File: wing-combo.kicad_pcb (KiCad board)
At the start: 2 copper layers, 93 x 91.3 mm, 118 parts, among them J1 Conn_01x03_Male, J10 Screw_Terminal_01x02, J11 Screw_Terminal_01x02, J12 Screw_Terminal_01x02, J13 USB_A, J14 Screw_Terminal_01x02, J15 Conn_02x16_Row_Letter_Last, J16 Conn_02x12_Row_Letter_Last, J5 Screw_Terminal_01x02, J6 Screw_Terminal_01x02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

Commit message: change URL on board to makehaven.org/toolauth, to match with Project name on GitHub
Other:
- board text added: "makehaven.org/toolauth"
- board text removed: "makehaven.org/openshop"
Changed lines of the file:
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@@
 		)
 	)
-	(gr_text "makehaven.org/openshop"
-		(at 68.435 53.46 90)
+	(gr_text "makehaven.org/toolauth"
+		(at 68.435 53.579828 90)
 		(layer "B.SilkS")
 		(effects

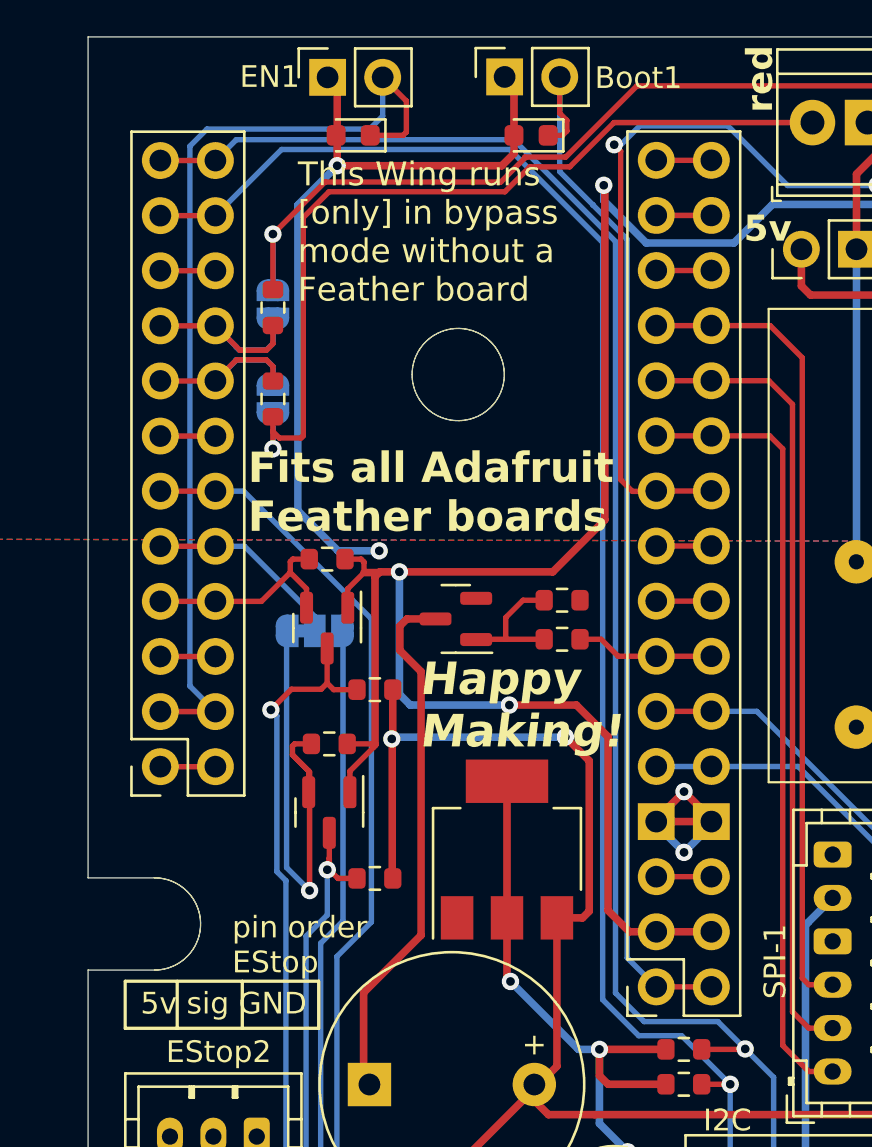
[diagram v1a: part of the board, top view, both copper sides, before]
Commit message: unpopulate headers that are not needed
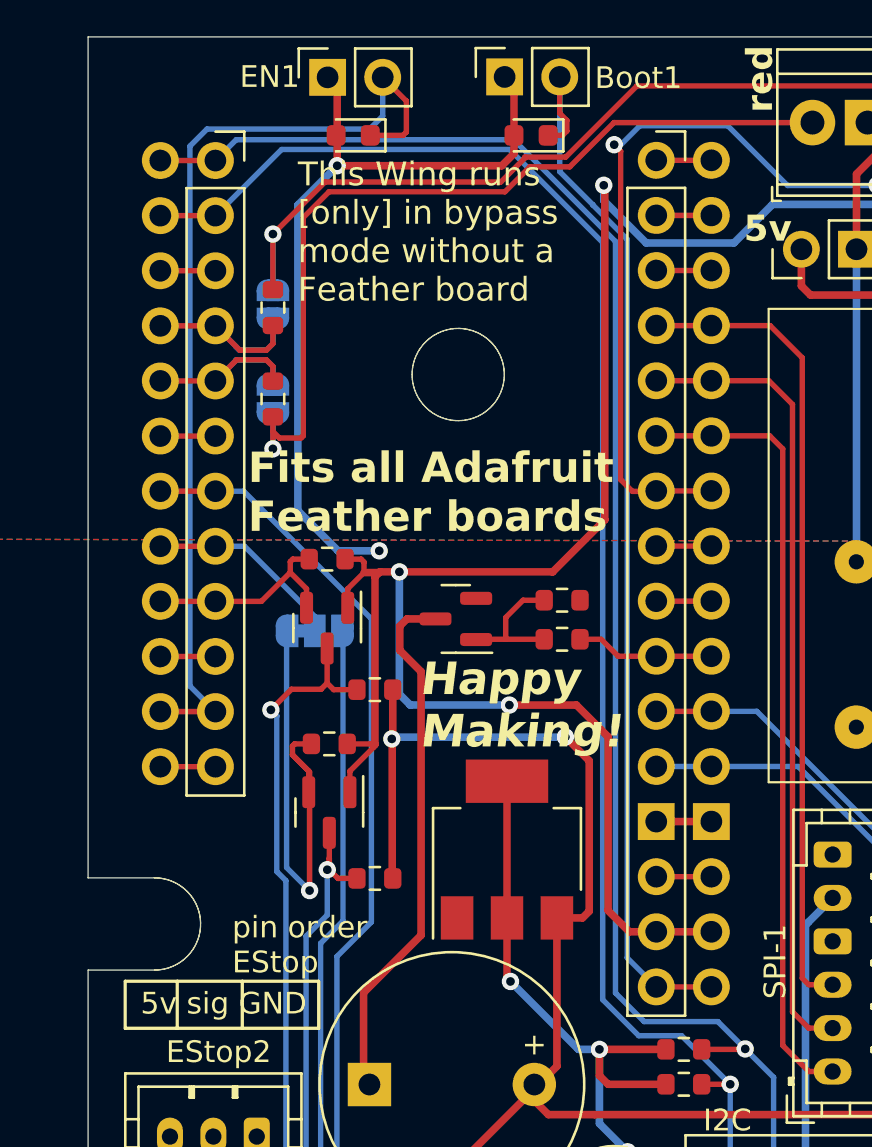
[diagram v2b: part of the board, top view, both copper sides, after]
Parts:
- added J3: Conn_01x12, Connector_PinSocket_2.54mm:PinSocket_1x12_P2.54mm_Vertical, F.Cu at (42.8, 28.6)
- added J4: Conn_01x12, Connector_PinSocket_2.54mm:PinSocket_1x12_P2.54mm_Vertical, F.Cu at (40.2, 28.6)
- IN-1: value 3.5mm -> H/L1
- IN-2: value 3.5mm -> N/L2
- IN-3: value 3.5mm -> VOLTS
- J15: value Conn_02x16_Row_Letter_Last -> Conn_01x16; footprint Connector_PinSocket_2.54mm:PinSocket_2x16_P2.54mm_Vertical -> Connector_PinSocket_2.54mm:PinSocket_1x16_P2.54mm_Vertical
- J16: value Conn_02x12_Row_Letter_Last -> Conn_01x16; footprint Connector_PinSocket_2.54mm:PinSocket_2x12_P2.54mm_Vertical -> Connector_PinSocket_2.54mm:PinSocket_1x16_P2.54mm_Vertical
- moved J15 38.2 mm to (65.6, 28.6), turned to 0 degrees
- moved J16 36.1 mm to (63.1, 28.6), turned to 0 degrees
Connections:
- J15 pad 1: boot -> Net-(J15-Pin_1)
- J15 pad 10: set3v -> buzz
- J15 pad 12: reset3v -> set3v
- J15 pad 13: buzz -> GND
- J15 pad 14: buzz -> Net-(J15-Pin_14)
- J15 pad 15: Net-(J15-Pin_15) -> +3.3VA
- J15 pad 16: Net-(J15-Pin_15) -> boot
- J15 pad 2: boot -> Net-(J15-Pin_2)
- J15 pad 3: +3.3VA -> Net-(J15-Pin_3)
- J15 pad 4: +3.3VA -> PICO
- J15 pad 5: Net-(J15-Pin_5) -> POCI
- J15 pad 6: Net-(J15-Pin_5) -> SCK
- J15 pad 7: GND -> 3vRead-Bypass
- J15 pad 8: GND -> Net-(J15-Pin_8)
- J15 pad 9: set3v -> Net-(J15-Pin_9)
- J16 pad 1: Net-(J16-Pin_1) -> Net-(J15-Pin_1)
- J16 pad 10: two-options -> buzz
- J16 pad 11: ade7953-IRQ -> reset3v
- J16 pad 12: ade7953-IRQ -> set3v
- J16 pad 13: Net-(J16-Pin_13) -> GND
- J16 pad 14: Net-(J16-Pin_13) -> Net-(J15-Pin_14)
- J16 pad 15: led-grn -> +3.3VA
- J16 pad 16: led-grn -> boot
- J16 pad 2: Net-(J16-Pin_1) -> Net-(J15-Pin_2)
- J16 pad 3: EN -> Net-(J15-Pin_3)
- J16 pad 4: EN -> PICO
- J16 pad 5: Net-(J16-Pin_5) -> POCI
- J16 pad 6: Net-(J16-Pin_5) -> SCK
- J16 pad 7: read-E-Stop -> 3vRead-Bypass
- J16 pad 8: read-E-Stop -> Net-(J15-Pin_8)
- J16 pad 9: two-options -> Net-(J15-Pin_9)
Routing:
- net GND: track 99.0 -> 91.6 mm, vias 9 -> 7
- net Net-(J15-Pin_9): track 0.00 -> 2.54 mm
- net Net-(J15-Pin_8): track 0.00 -> 2.54 mm
- net Net-(J15-Pin_5): track 2.54 -> 0.00 mm
- net Net-(J15-Pin_31): track 2.54 -> 0.00 mm
- net Net-(J15-Pin_3): track 0.00 -> 2.54 mm
- net Net-(J15-Pin_29): track 2.54 -> 0.00 mm
- net Net-(J15-Pin_27): track 2.54 -> 0.00 mm
- net Net-(J15-Pin_2): track 0.00 -> 2.54 mm
- net Net-(J15-Pin_17): track 2.54 -> 0.00 mm
- net Net-(J15-Pin_15): track 2.54 -> 0.00 mm
- net Net-(J15-Pin_14): track 0.00 -> 2.54 mm
- net Net-(J15-Pin_1): track 0.00 -> 2.54 mm
- net Net-(J3-Pin_6): track 0.00 -> 2.54 mm
- net Net-(J3-Pin_3): track 0.00 -> 2.54 mm
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
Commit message: convert to new parts on the board: footprint change for relay and wishlist-JST connectors
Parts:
- removed Boot1: Conn_01x02_Female, Connector_PinSocket_2.54mm:PinSocket_1x02_P2.54mm_Vertical
- removed J1: Conn_01x03_Male, TerminalBlock_TE-Connectivity:TerminalBlock_TE_282834-3_1x03_P2.54mm_Horizontal
- added R-G-LED1: Conn_01x03_Female, Connector_JST:JST_PH_B3B-PH-K_1x03_P2.00mm_Vertical, F.Cu at (71.4, 25.4)
- added boot1: Conn_01x02_Female, Connector_JST:JST_PH_S2B-PH-K_1x02_P2.00mm_Horizontal, F.Cu at (57.7, 29.9)
- EN1: footprint Connector_PinSocket_2.54mm:PinSocket_1x02_P2.54mm_Vertical -> Connector_JST:JST_PH_S2B-PH-K_1x02_P2.00mm_Horizontal
- R31: footprint MY2-02 AC110 Omron:relay-Omron-MY2-02 -> j1512cp120vac1.2:relay-J1512CP120VAC
- moved EN1 5.49 mm to (49.9, 29.9), turned to 180 degrees
- moved C1 5.14 mm to (56.7, 32.5)
- moved C2 5.10 mm to (48.9, 32.5)
- moved R31 1.47 mm to (99.1, 102.1), turned to 90 degrees
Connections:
- EN1 pad 1: GND -> EN
- EN1 pad 2: EN -> GND
- SPI-1 pad 4: GND -> unconnected-(SPI-1-Pin_4-Pad4)
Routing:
- net 3vRead-Bypass: track 42.0 -> 28.9 mm, vias 2 -> 0
- net EN: track 45.0 -> 38.8 mm
- net Net-(JP16-B): track 40.5 -> 46.5 mm
- net Net-(JP15-B): track 39.4 -> 43.4 mm
- net +3.3VA: track 95.4 -> 92.4 mm
- net SDA: track 101.5 -> 103.0 mm
- net SCL: track 102.5 -> 104.0 mm
- net GND: track 91.6 -> 91.1 mm
- net +5V: track 201.3 -> 201.7 mm, vias 2 -> 3
- net boot: track 49.9 -> 50.1 mm, vias 0 -> 1
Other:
- board text added: "Designers: Corey Rice, Iris Artin,"
- board text added: "bypass [only] without feather"
- board text removed: "Designed by: Corey Rice, Iris Artin,"
- board text removed: "This Wing runs [only] in bypass mode without a Feather board"
- board text removed: "green"

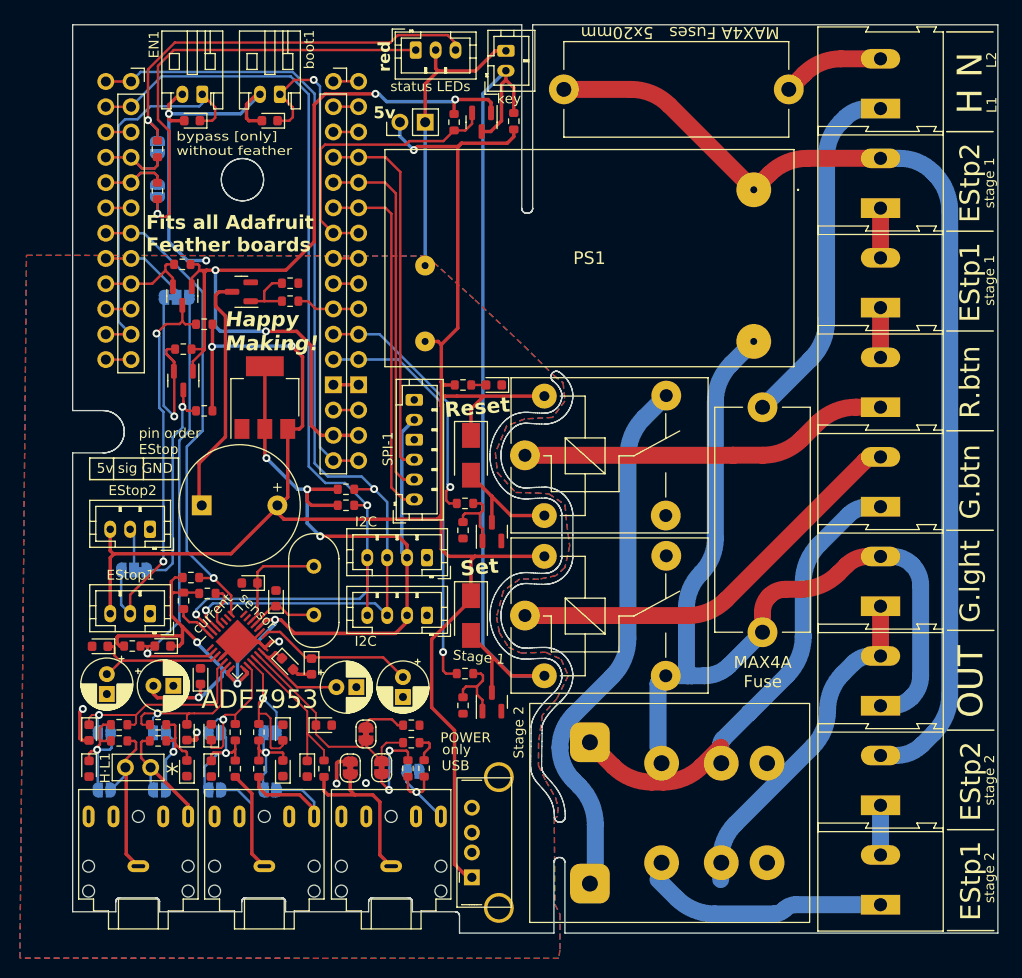
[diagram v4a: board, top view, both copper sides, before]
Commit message: placed new screw terminals on board
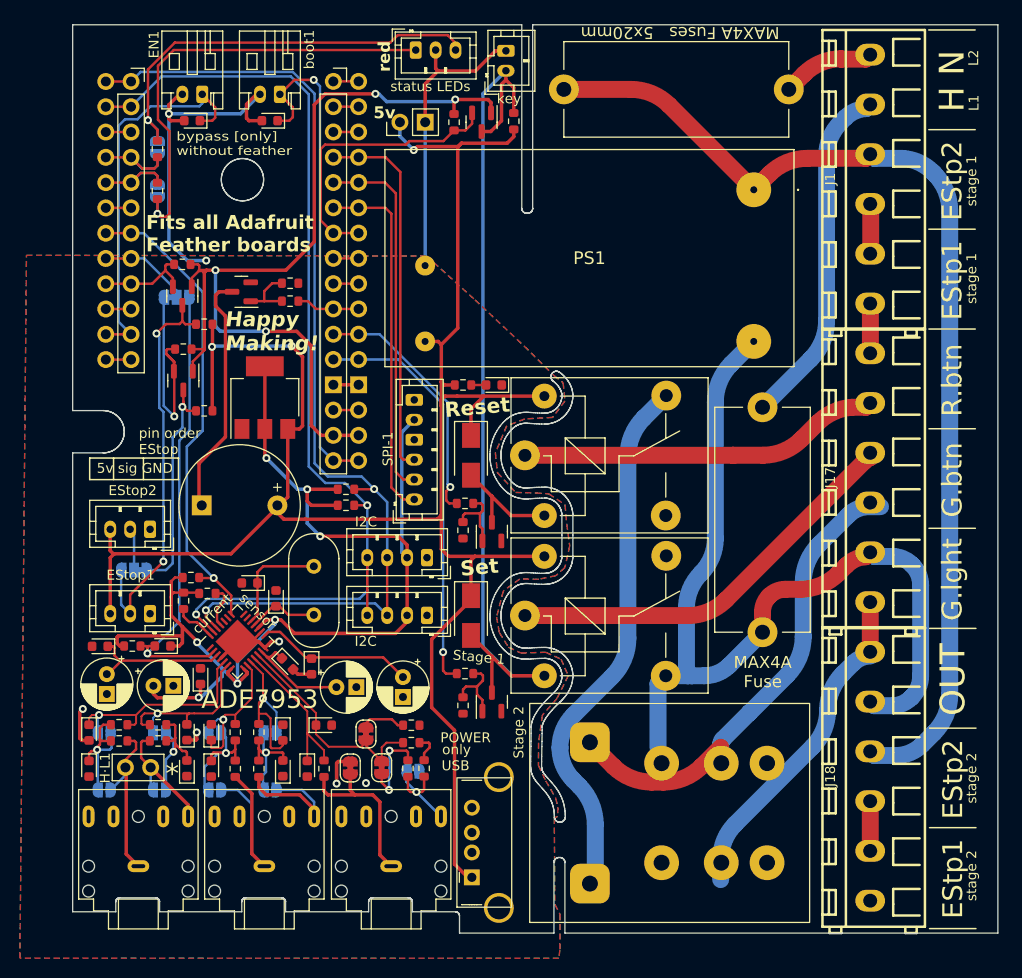
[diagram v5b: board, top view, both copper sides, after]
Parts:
- removed J10, J11, J12, J14, J5, J6, J7, J8, J9: Screw_Terminal_01x02, TerminalBlock:TerminalBlock_Altech_AK300-2_P5.00mm
- added J1: Screw_Terminal_01x06, screw_terminal:CONN-TH_6P-P5.00_MX128-5.0-06P-GN01-CU-Y-A, F.Cu at (117.0, 38.4)
- added J17: Screw_Terminal_01x06, screw_terminal:CONN-TH_6P-P5.00_MX128-5.0-06P-GN01-CU-Y-A, F.Cu at (117.0, 68.4)
- added J18: Screw_Terminal_01x06, screw_terminal:CONN-TH_6P-P5.00_MX128-5.0-06P-GN01-CU-Y-A, F.Cu at (117.0, 98.4)
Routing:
- net Member-E-Stop-sw1-1: track 23.8 -> 0.00 mm
- net Green-Indicator-light-1: track 91.7 -> 93.3 mm
- net Member-E-Stop-aux2-2: track 105.7 -> 107.3 mm
- net Green-Indicator-light-2: track 34.4 -> 33.4 mm
- net H/L1: track 35.8 -> 34.9 mm
- net Member-Red-Reset-Button-1: track 37.2 -> 36.4 mm
- net N/L2: track 10.2 -> 9.40 mm
- net Member-Green-Button-1: track 42.0 -> 41.4 mm
